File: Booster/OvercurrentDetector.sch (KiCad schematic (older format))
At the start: 34 parts

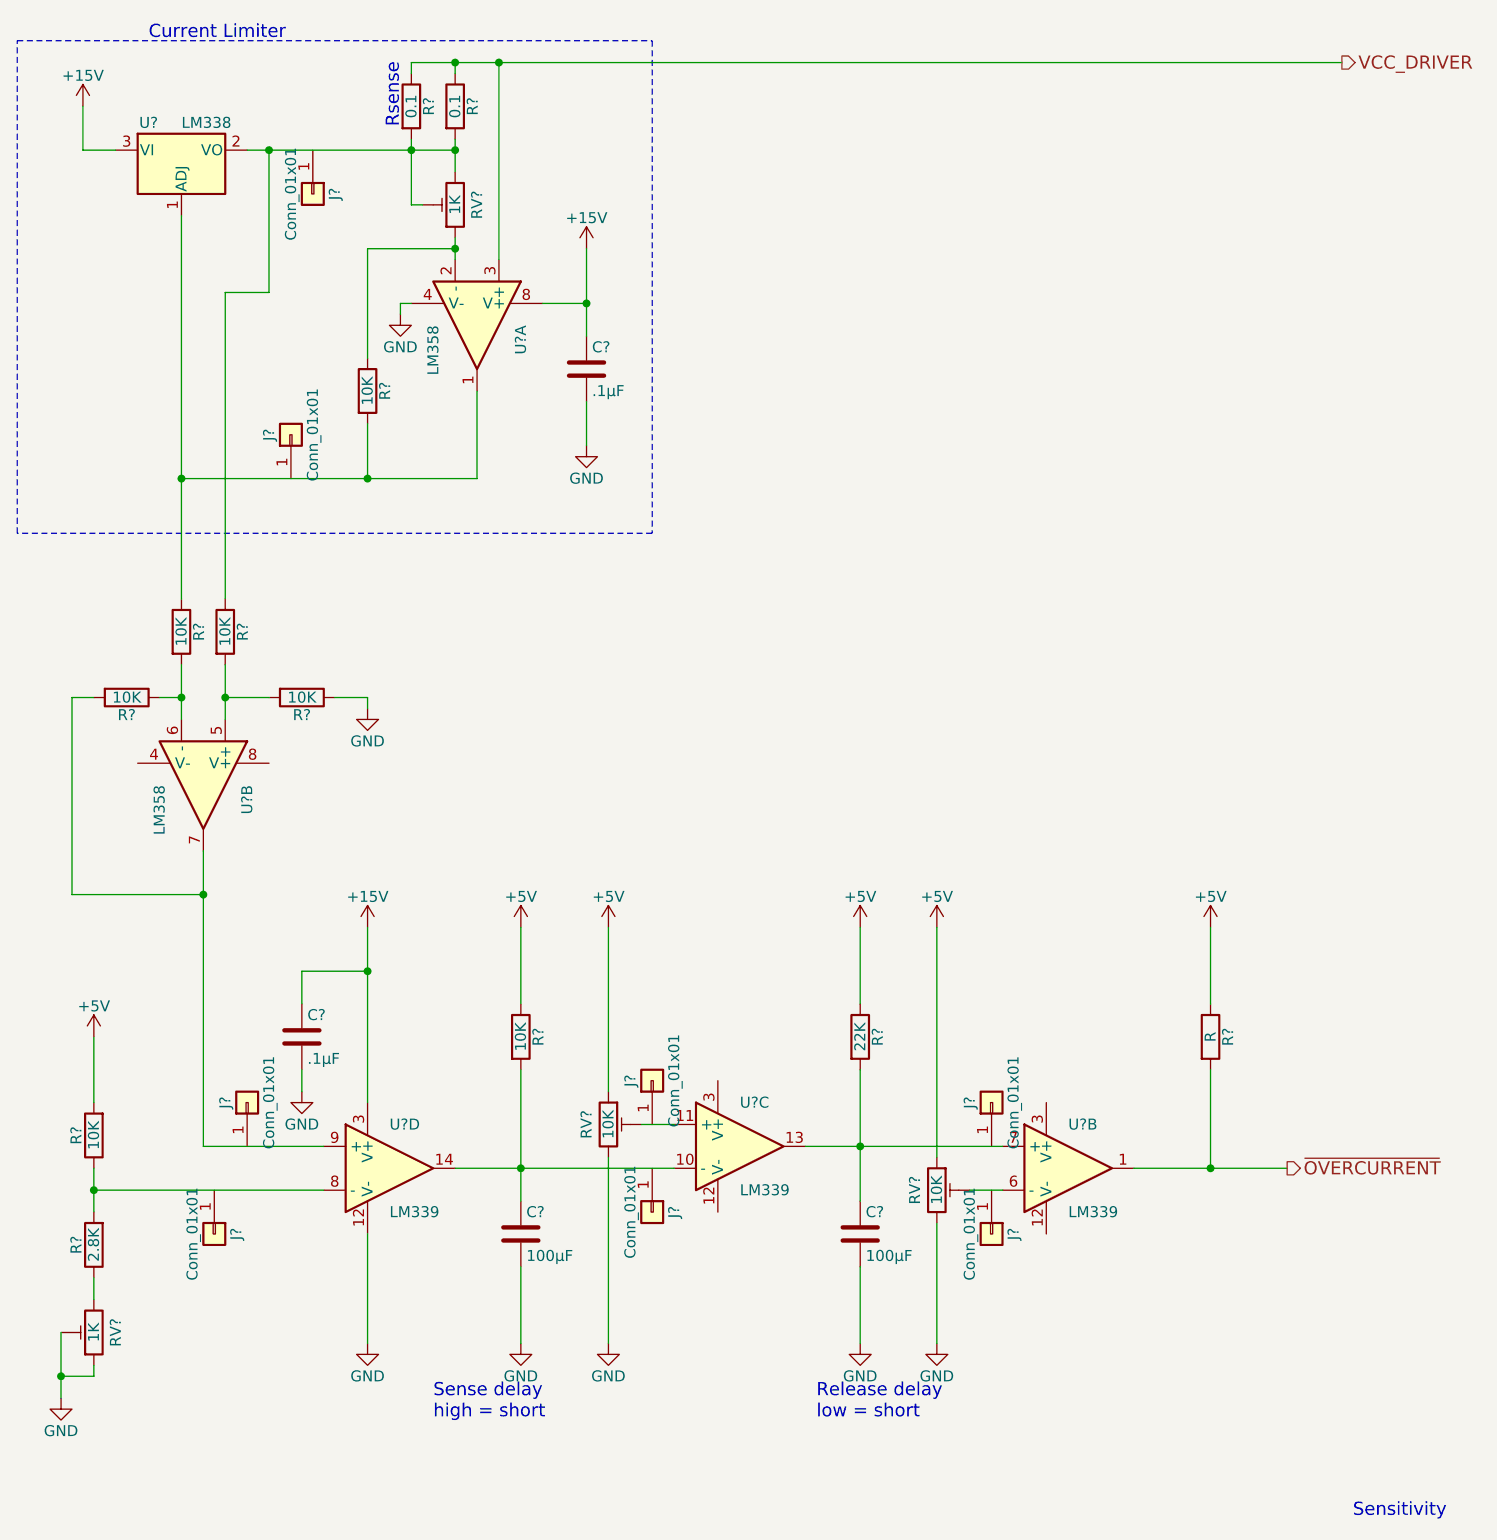
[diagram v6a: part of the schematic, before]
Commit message: Use actual test point instead of 1 pin jumpers.
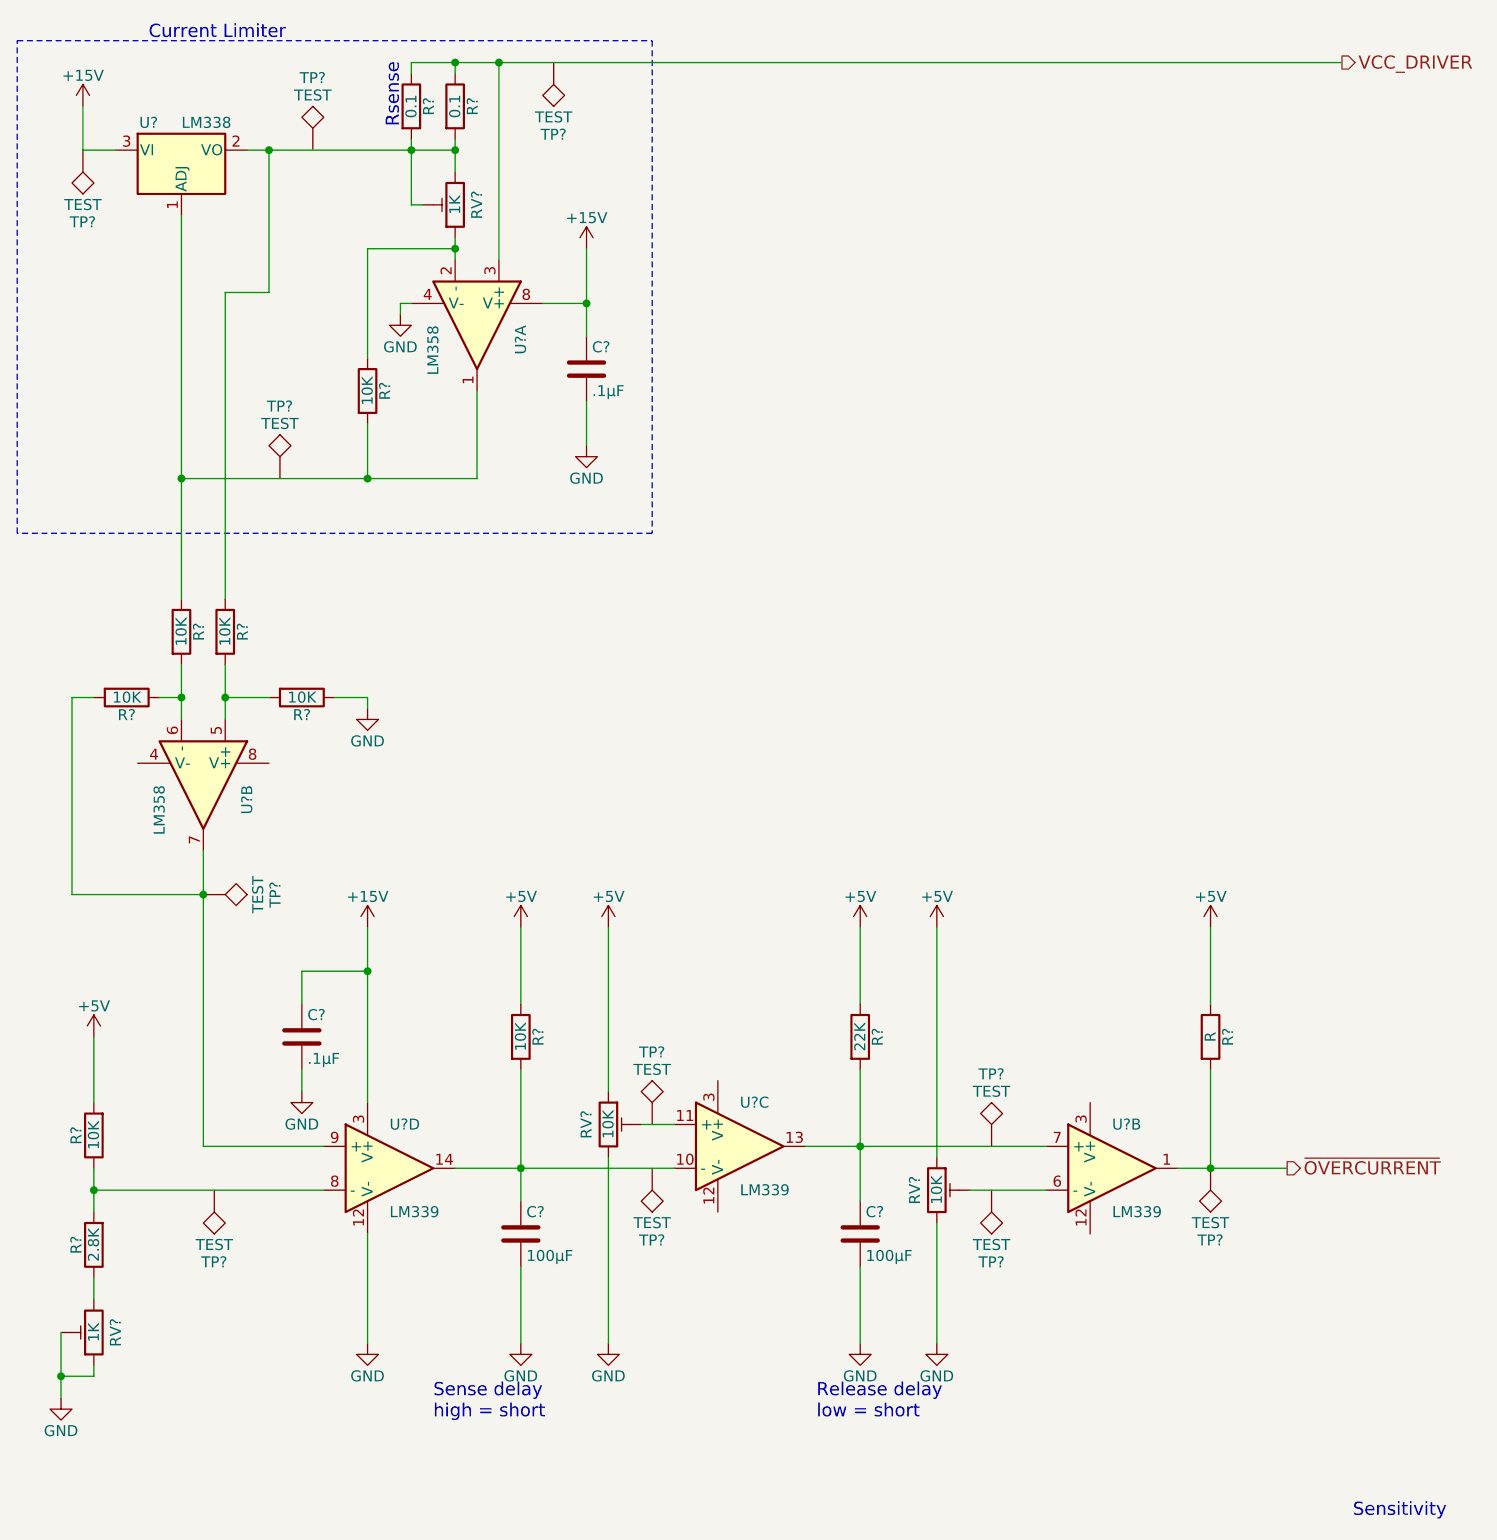
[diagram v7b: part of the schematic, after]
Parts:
- removed J? (x8): Conn_01x01, symbol Conn_01x01
- added TP? (x11): TEST, symbol TEST
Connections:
- net +15V: now also TP?.1
- net ~OVERCURRENT: now also TP?.1
- net at R?.2, U?.7, U?.9 (+): now also TP?.1
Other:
- moved on the sheet: U?B

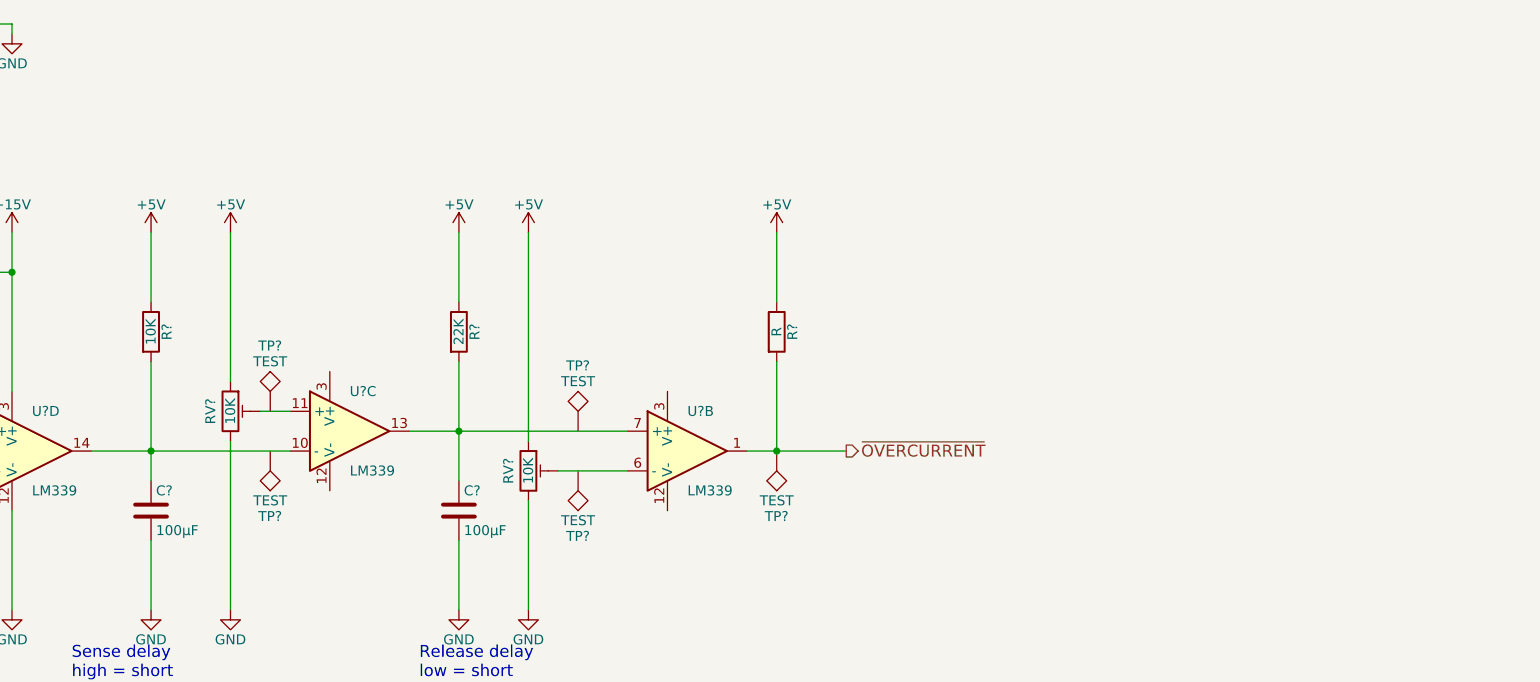
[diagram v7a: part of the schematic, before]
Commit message: Minor fixes based on breadboard experiments.
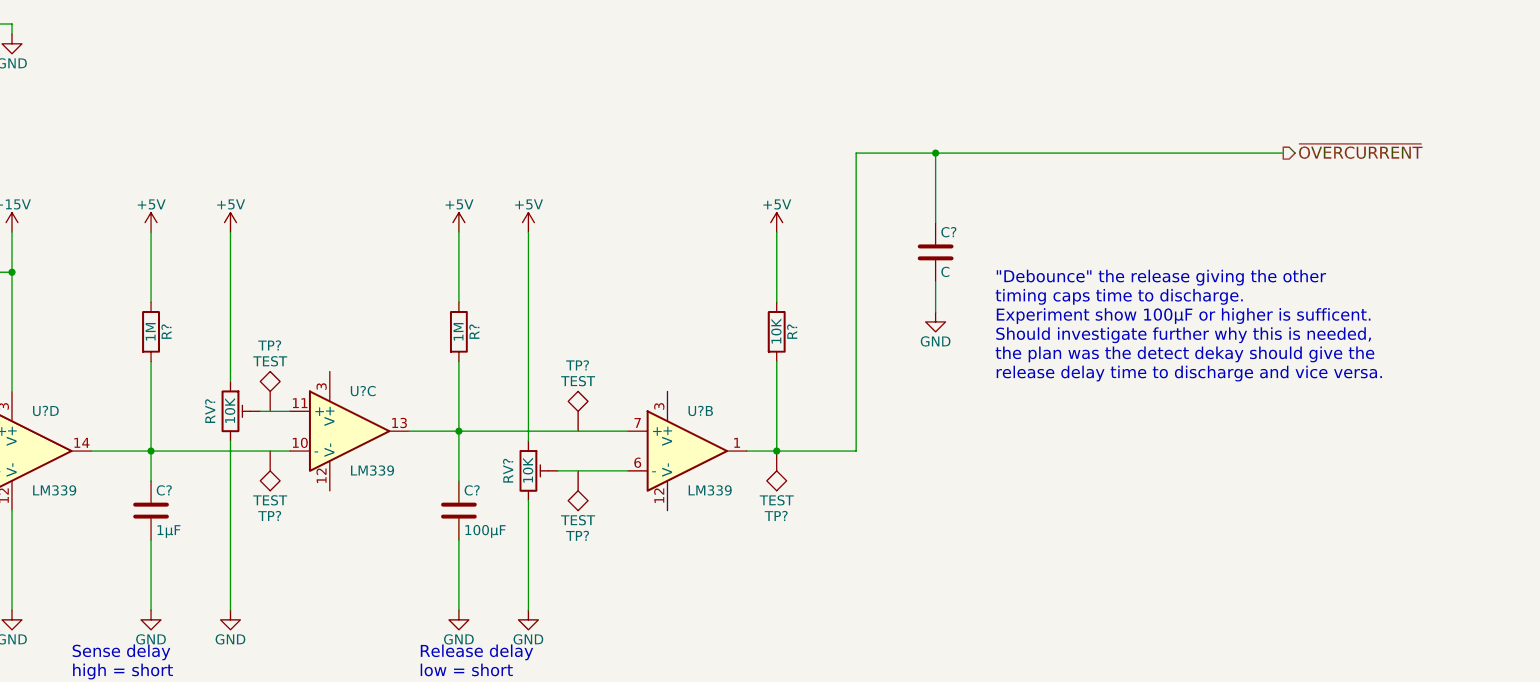
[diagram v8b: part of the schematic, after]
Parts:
- added C?: C, symbol C
- C?: value 100µF -> 1µF
- R?: value 10K -> 1M
- R?: value 22K -> 1M
- R?: value R -> 10K
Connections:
- net GND: now also C?.2
- net ~OVERCURRENT: now also C?.1
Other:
- note added: ""Debounce" the release giving the other\ntiming caps time to discharge.\nExperiment show 100µF or higher is sufficent.\nShould investigate further why this is needed,\nthe plan was the detect dekay should give the\nrelease delay time to discharge and vice versa."
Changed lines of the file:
@@
 Comment4 ""
 $EndDescr
-Text HLabel 8100 6050 2    60   Output ~ 0
+Text HLabel 10300 4550 2    60   Output ~ 0
 ~OVERCURRENT
 $Comp
@@
 P 4600 6350
 F 0 "C?" H 4625 6450 50  0000 L CNN
-F 1 "100µF" H 4625 6250 50  0000 L CNN
+F 1 "1µF" H 4625 6250 50  0000 L CNN
 F 2 "" H 4638 6200 50  0001 C CNN
 F 3 "" H 4600 6350 50  0001 C CNN
@@
 P 4600 5450
 F 0 "R?" V 4680 5450 50  0000 C CNN
-F 1 "10K" V 4600 5450 50  0000 C CNN
+F 1 "1M" V 4600 5450 50  0000 C CNN
 F 2 "" V 4530 5450 50  0000 C CNN
 F 3 "" H 4600 5450 50  0000 C CNN
@@
 P 6150 5450
 F 0 "R?" V 6230 5450 50  0000 C CNN
-F 1 "22K" V 6150 5450 50  0000 C CNN
+F 1 "1M" V 6150 5450 50  0000 C CNN
 F 2 "" V 6080 5450 50  0000 C CNN
 F 3 "" H 6150 5450 50  0000 C CNN
@@
 P 7750 5450
 F 0 "R?" V 7830 5450 50  0000 C CNN
-F 1 "R" V 7750 5450 50  0000 C CNN
+F 1 "10K" V 7750 5450 50  0000 C CNN
 F 2 "" V 7680 5450 50  0000 C CNN
 F 3 "" H 7750 5450 50  0000 C CNN
@@
 	7600 6050 7750 6050
 Wire Wire Line
-	7750 6050 8100 6050
+	7750 6050 8150 6050
 Wire Wire Line
 	7750 6050 7750 5600
@@
 	-1   0    0    1
 $EndComp
+Wire Wire Line
+	8150 6050 8150 4550
+Wire Wire Line
+	8150 4550 8550 4550
+Wire Wire Line
+	8550 4550 10300 4550
+Wire Wire Line
+	8550 4550 8550 4900
+Connection ~ 8550 4550
+$Comp
+L C C?
+U 1 1 5A19D624
+P 8550 5050
+F 0 "C?" H 8575 5150 50  0000 L CNN
+F 1 "C" H 8575 4950 50  0000 L CNN
+F 2 "" H 8588 4900 50  0000 C CNN
+F 3 "" H 8550 5050 50  0000 C CNN
+	1    8550 5050
+	1    0    0    -1
+$EndComp
+Wire Wire Line
+	8550 5200 8550 5350
+$Comp
+L GND #PWR?
+U 1 1 5A19D713
+P 8550 5350
+F 0 "#PWR?" H 8550 5100 50  0001 C CNN
+F 1 "GND" H 8550 5200 50  0000 C CNN
+F 2 "" H 8550 5350 50  0000 C CNN
+F 3 "" H 8550 5350 50  0000 C CNN
+	1    8550 5350
+	1    0    0    -1
+$EndComp
+Text Notes 8850 5700 0    60   ~ 0
+"Debounce" the release giving the other\ntiming caps time to discharge.\nExperiment show 100µF or higher is sufficent.\nShould investigate further why this is needed,\nthe plan was the detect dekay should give the\nrelease delay time to discharge and vice versa.
 $EndSCHEMATC
